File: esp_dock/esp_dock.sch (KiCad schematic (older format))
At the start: 8 parts, among them P1 CONN_01X02, P2 CONN_01X04, P3 CONN_02X04, SW1 Switch_SPDT_x2, U1 LM3671

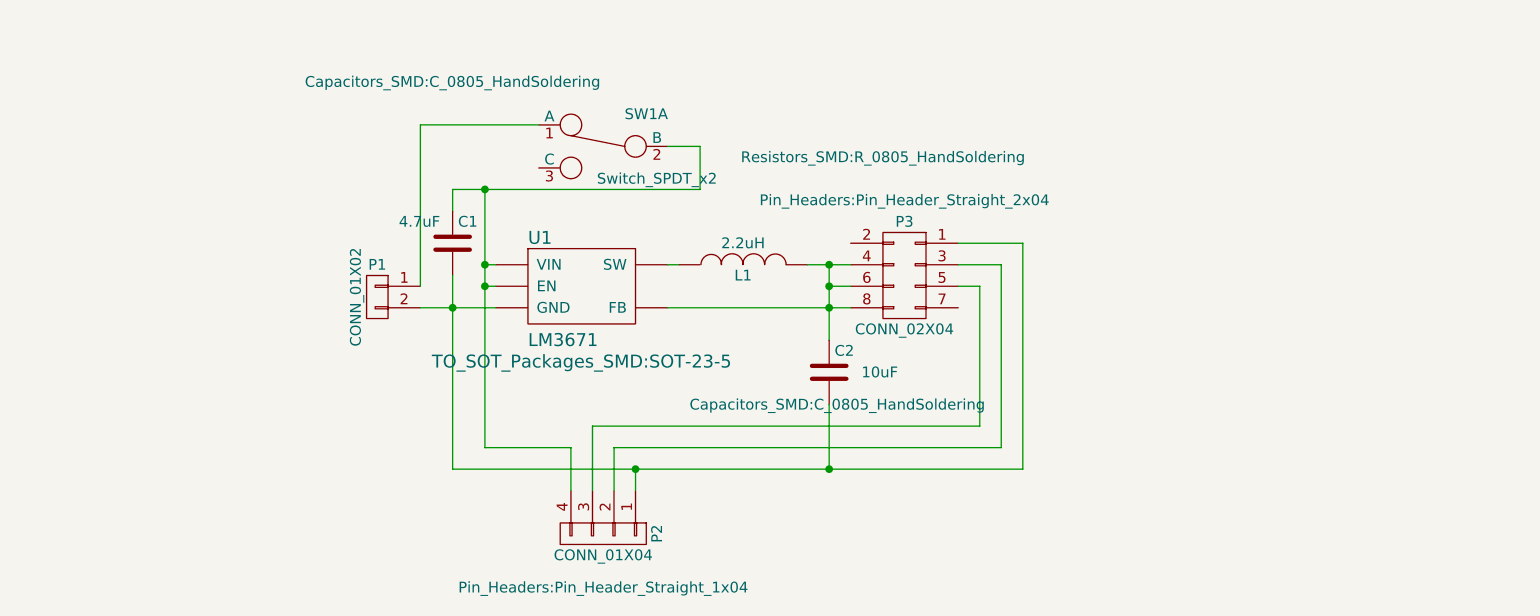
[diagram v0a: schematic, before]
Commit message: Set up footprints for esp dock
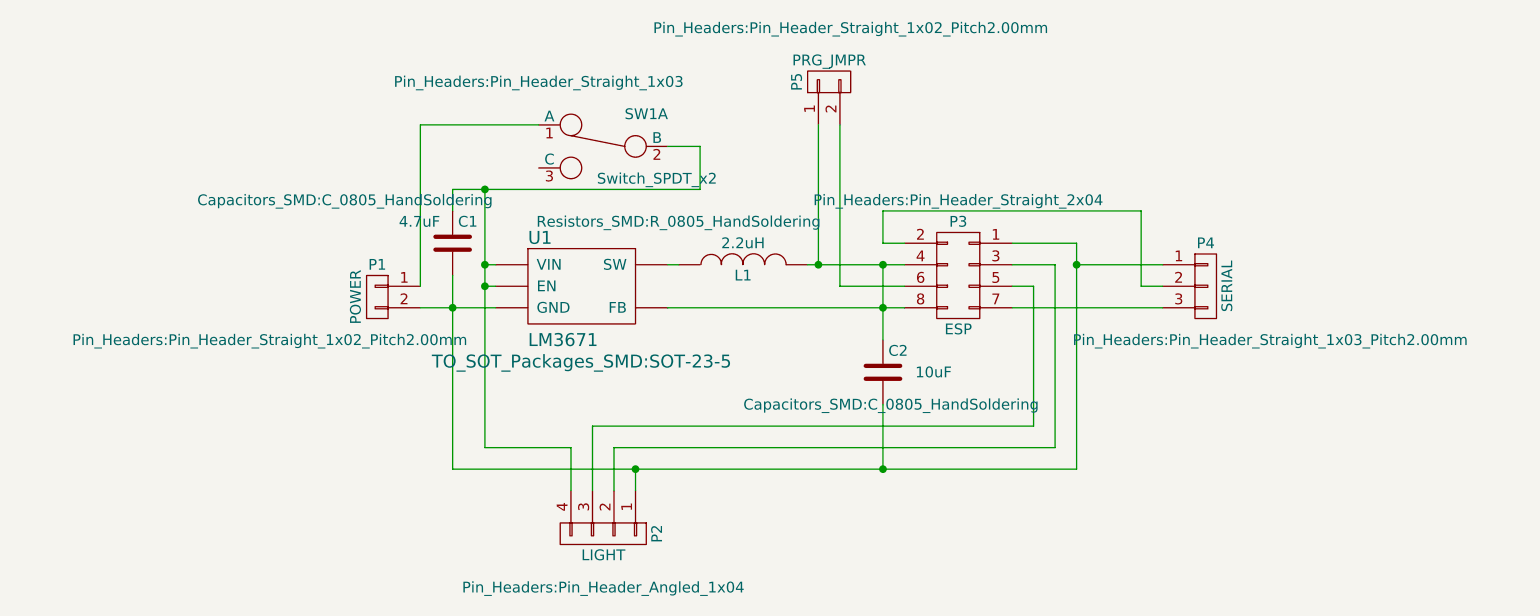
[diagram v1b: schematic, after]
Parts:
- added P4: SERIAL, Pin_Headers:Pin_Header_Straight_1x03_Pitch2.00mm, symbol CONN_01X03
- added P5: PRG_JMPR, Pin_Headers:Pin_Header_Straight_1x02_Pitch2.00mm, symbol CONN_01X02
- P1: value CONN_01X02 -> POWER; footprint (none) -> Pin_Headers:Pin_Header_Straight_1x02_Pitch2.00mm
- P2: value CONN_01X04 -> LIGHT; footprint Pin_Headers:Pin_Header_Straight_1x04 -> Pin_Headers:Pin_Header_Angled_1x04
- P3: value CONN_02X04 -> ESP
- SW1: footprint (none) -> Pin_Headers:Pin_Header_Straight_1x03
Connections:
- net at C1.2, C2.2, P1.2 (P2)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: now also P4.1 (P1)
- net at C2.1, L1.2, P3.4 (P4)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: now also P5.1 (P1); no longer P3.6 (P6)
- net at P3.2 (P2): now also P4.2 (P2)
- net at P3.7 (P7): now also P4.3 (P3)
- new net: P3.6 (P6), P5.2 (P2)
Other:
- moved on the sheet: C2, P3
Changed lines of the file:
@@
 F 0 "SW1" H 6050 3250 50  0000 C CNN
 F 1 "Switch_SPDT_x2" H 6000 2950 50  0000 C CNN
-F 2 "" H 6250 3100 50  0000 C CNN
+F 2 "Pin_Headers:Pin_Header_Straight_1x03" H 6550 3400 50  0000 C CNN
 F 3 "" H 6250 3100 50  0000 C CNN
 	1    6250 3100
@@
 P 5200 3800
 F 0 "P1" H 5200 3950 50  0000 C CNN
-F 1 "CONN_01X02" V 5300 3800 50  0000 C CNN
-F 2 "" H 5200 3800 50  0000 C CNN
+F 1 "POWER" V 5300 3800 50  0000 C CNN
+F 2 "Pin_Headers:Pin_Header_Straight_1x02_Pitch2.00mm" H 5700 3600 50  0000 C CNN
 F 3 "" H 5200 3800 50  0000 C CNN
 	1    5200 3800
@@
 P 6250 4900
 F 0 "P2" H 6250 5150 50  0000 C CNN
-F 1 "CONN_01X04" V 6350 4900 50  0000 C CNN
-F 2 "Pin_Headers:Pin_Header_Straight_1x04" V 6500 4900 50  0000 C CNN
+F 1 "LIGHT" V 6350 4900 50  0000 C CNN
+F 2 "Pin_Headers:Pin_Header_Angled_1x04" V 6500 4900 50  0000 C CNN
 F 3 "" H 6250 4900 50  0000 C CNN
 	1    6250 4900
 	0    1    1    0
+$EndComp
+$Comp
+L INDUCTOR L1
+U 1 1 57A0E1B1
+P 6900 3650
+F 0 "L1" V 6850 3650 50  0000 C CNN
+F 1 "2.2uH" V 7000 3650 50  0000 C CNN
+F 2 "Resistors_SMD:R_0805_HandSoldering" V 7100 3950 50  0000 C CNN
+F 3 "" H 6900 3650 50  0000 C CNN
+	1    6900 3650
+	0    -1   -1   0
+$EndComp
+$Comp
+L C C2
+U 1 1 57A0E396
+P 7550 4150
+F 0 "C2" H 7575 4250 50  0000 L CNN
+F 1 "10uF" H 7700 4150 50  0000 L CNN
+F 2 "Capacitors_SMD:C_0805_HandSoldering" H 7588 4000 50  0000 C CNN
+F 3 "" H 7550 4150 50  0000 C CNN
+	1    7550 4150
+	1    0    0    -1
+$EndComp
+$Comp
+L C C1
+U 1 1 57A0E3BE
+P 5550 3550
+F 0 "C1" H 5575 3650 50  0000 L CNN
+F 1 "4.7uF" H 5300 3650 50  0000 L CNN
+F 2 "Capacitors_SMD:C_0805_HandSoldering" H 5050 3750 50  0000 C CNN
+F 3 "" H 5550 3550 50  0000 C CNN
+	1    5550 3550
+	1    0    0    -1
+$EndComp
+$Comp
+L CONN_02X04 P3
+U 1 1 57B3FBD7
+P 7900 3700
+F 0 "P3" H 7900 3950 50  0000 C CNN
+F 1 "ESP" H 7900 3450 50  0000 C CNN
+F 2 "Pin_Headers:Pin_Header_Straight_2x04" H 7900 4050 50  0000 C CNN
+F 3 "" H 7900 2500 50  0000 C CNN
+	1    7900 3700
+	-1   0    0    -1
 $EndComp
 Wire Wire Line
@@
 	6550 3100 6700 3100
 Wire Wire Line
-	5700 3300 5700 3650
-Wire Wire Line
-	5700 3650 5700 3750
-Wire Wire Line
-	5700 3750 5700 4500
+	5700 3300 5700 4500
 Wire Wire Line
 	5700 3650 5750 3650
@@
 Connection ~ 5700 3650
 Wire Wire Line
-	5400 3850 5550 3850
+	5400 3850 5750 3850
 Wire Wire Line
-	5550 3850 5750 3850
+	5550 3700 5550 4600
 Wire Wire Line
-	5550 3700 5550 3850
-Wire Wire Line
-	5550 3850 5550 4600
-Wire Wire Line
-	5550 4600 6400 4600
-Wire Wire Line
-	6400 4600 7300 4600
-Wire Wire Line
-	7300 4600 8200 4600
+	5550 4600 8450 4600
 Wire Wire Line
 	6400 4600 6400 4700
 Connection ~ 5550 3850
-$Comp
-L INDUCTOR L1
-U 1 1 57A0E1B1
-P 6900 3650
-F 0 "L1" V 6850 3650 50  0000 C CNN
-F 1 "2.2uH" V 7000 3650 50  0000 C CNN
-F 2 "Resistors_SMD:R_0805_HandSoldering" V 7400 3000 50  0000 C CNN
-F 3 "" H 6900 3650 50  0000 C CNN
-	1    6900 3650
-	0    -1   -1   0
-$EndComp
 Wire Wire Line
 	6550 3650 6600 3650
-$Comp
-L C C2
-U 1 1 57A0E396
-P 7300 4150
-F 0 "C2" H 7325 4250 50  0000 L CNN
-F 1 "10uF" H 7450 4150 50  0000 L CNN
-F 2 "Capacitors_SMD:C_0805_HandSoldering" H 7338 4000 50  0000 C CNN
-F 3 "" H 7300 4150 50  0000 C CNN
-	1    7300 4150
-	1    0    0    -1
-$EndComp
-$Comp
-L C C1
-U 1 1 57A0E3BE
-P 5550 3550
-F 0 "C1" H 5575 3650 50  0000 L CNN
-F 1 "4.7uF" H 5300 3650 50  0000 L CNN
-F 2 "Capacitors_SMD:C_0805_HandSoldering" H 5550 4300 50  0000 C CNN
-F 3 "" H 5550 3550 50  0000 C CNN
-	1    5550 3550
-	1    0    0    -1
-$EndComp
 Wire Wire Line
-	6700 3300 6700 3100
+	6700 3100 6700 3300
 Wire Wire Line
-	5550 3300 5700 3300
-Wire Wire Line
-	5700 3300 6700 3300
+	6700 3300 5550 3300
 Wire Wire Line
 	5550 3300 5550 3400
 Connection ~ 5700 3300
 Wire Wire Line
-	7300 3650 7300 3750
+	7550 3650 7550 4000
 Wire Wire Line
-	7300 3750 7300 3850
+	6550 3850 7650 3850
+Connection ~ 7550 3850
 Wire Wire Line
-	7300 3850 7300 4000
-Wire Wire Line
-	6550 3850 7300 3850
-Wire Wire Line
-	7300 3850 7400 3850
-Connection ~ 7300 3850
-Wire Wire Line
-	7300 4600 7300 4300
+	7550 4600 7550 4300
 Connection ~ 6400 4600
 Wire Wire Line
@@
 Connection ~ 5700 3750
 Wire Wire Line
-	7200 3650 7300 3650
+	7200 3650 7650 3650
 Wire Wire Line
-	7300 3650 7400 3650
+	8150 3550 8450 3550
 Wire Wire Line
-	7900 3550 8200 3550
+	8450 3550 8450 4600
+Connection ~ 7550 4600
 Wire Wire Line
-	8200 3550 8200 4600
-Connection ~ 7300 4600
+	8250 3750 8250 4400
 Wire Wire Line
-	8000 3750 8000 4400
+	8250 3750 8150 3750
 Wire Wire Line
-	8000 3750 7900 3750
-Wire Wire Line
-	8000 4400 6200 4400
+	8250 4400 6200 4400
 Wire Wire Line
 	6200 4400 6200 4700
 Wire Wire Line
-	7900 3650 8100 3650
+	8150 3650 8350 3650
 Wire Wire Line
-	8100 3650 8100 4500
+	8350 3650 8350 4500
 Wire Wire Line
-	8100 4500 6300 4500
+	8350 4500 6300 4500
 Wire Wire Line
 	6300 4500 6300 4700
-Connection ~ 7300 3650
+Connection ~ 7550 3650
 Wire Wire Line
-	7400 3750 7300 3750
-Connection ~ 7300 3750
+	8150 3850 8850 3850
+Wire Wire Line
+	7650 3550 7550 3550
+Wire Wire Line
+	7550 3550 7550 3400
+Wire Wire Line
+	7550 3400 8750 3400
+Wire Wire Line
+	8750 3400 8750 3750
+Wire Wire Line
+	8750 3750 8850 3750
+Wire Wire Line
+	8850 3650 8450 3650
+Connection ~ 8450 3650
 $Comp
-L CONN_02X04 P3
-U 1 1 57B3FBD7
-P 7650 3700
-F 0 "P3" H 7650 3950 50  0000 C CNN
-F 1 "CONN_02X04" H 7650 3450 50  0000 C CNN
-F 2 "Pin_Headers:Pin_Header_Straight_2x04" H 7650 4050 50  0000 C CNN
-F 3 "" H 7650 2500 50  0000 C CNN
-	1    7650 3700
-	-1   0    0    -1
+L CONN_01X03 P4
+U 1 1 584F7038
+P 9050 3750
+F 0 "P4" H 9050 3950 50  0000 C CNN
+F 1 "SERIAL" V 9150 3750 50  0000 C CNN
+F 2 "Pin_Headers:Pin_Header_Straight_1x03_Pitch2.00mm" H 9350 3500 50  0000 C CNN
+F 3 "" H 9050 3750 50  0000 C CNN
+	1    9050 3750
+	1    0    0    -1
 $EndComp
+$Comp
+L CONN_01X02 P5
+U 1 1 584F74ED
+P 7300 2800
+F 0 "P5" H 7300 2950 50  0000 C CNN
+F 1 "PRG_JMPR" V 7400 2800 50  0000 C CNN
+F 2 "Pin_Headers:Pin_Header_Straight_1x02_Pitch2.00mm" V 7550 2700 50  0000 C CNN
+F 3 "" H 7300 2800 50  0000 C CNN
+	1    7300 2800
+	0    -1   -1   0
+$EndComp
+Wire Wire Line
+	7650 3750 7350 3750
+Wire Wire Line
+	7350 3750 7350 3000
+Wire Wire Line
+	7250 3000 7250 3650
+Connection ~ 7250 3650
 $EndSCHEMATC
